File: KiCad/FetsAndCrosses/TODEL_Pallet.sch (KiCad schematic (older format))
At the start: 2 parts, among them Q1 BSS84, Q2 2N7002

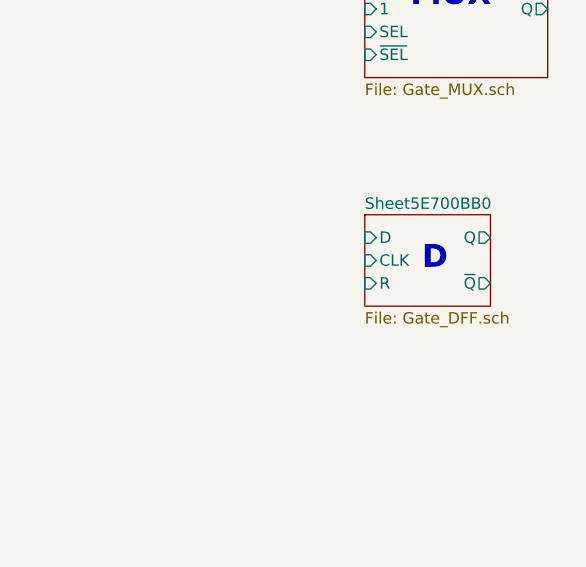
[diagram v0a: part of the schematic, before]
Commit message: Reworked everything to use Buses
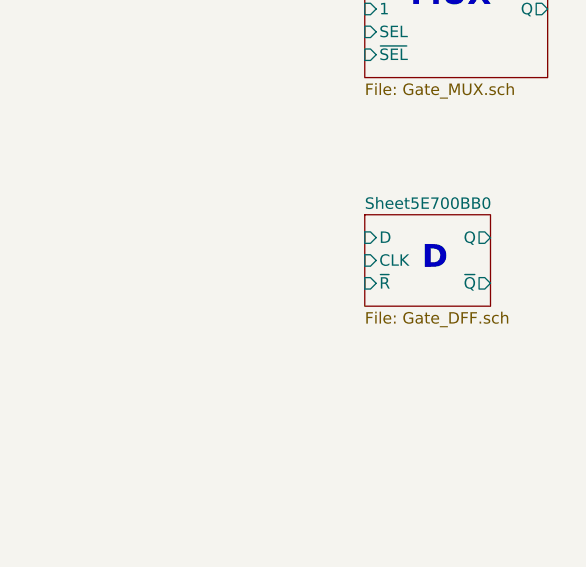
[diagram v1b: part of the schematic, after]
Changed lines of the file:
@@
 $Descr A4 11693 8268
 encoding utf-8
-Sheet 169 215
+Sheet 131 400
 Title ""
 Date ""
@@
 F2 "D" I L 8200 2100 50
 F3 "CLK" I L 8200 2200 50
-F4 "R" I L 8200 2300 50
-F5 "Q" O R 8750 2100 50
-F6 "~Q" O R 8750 2300 50
+F4 "Q" O R 8750 2100 50
+F5 "~Q" O R 8750 2300 50
+F6 "~R" I L 8200 2300 50
 $EndSheet
 Text Notes 8400 1100 0    100  ~ 20

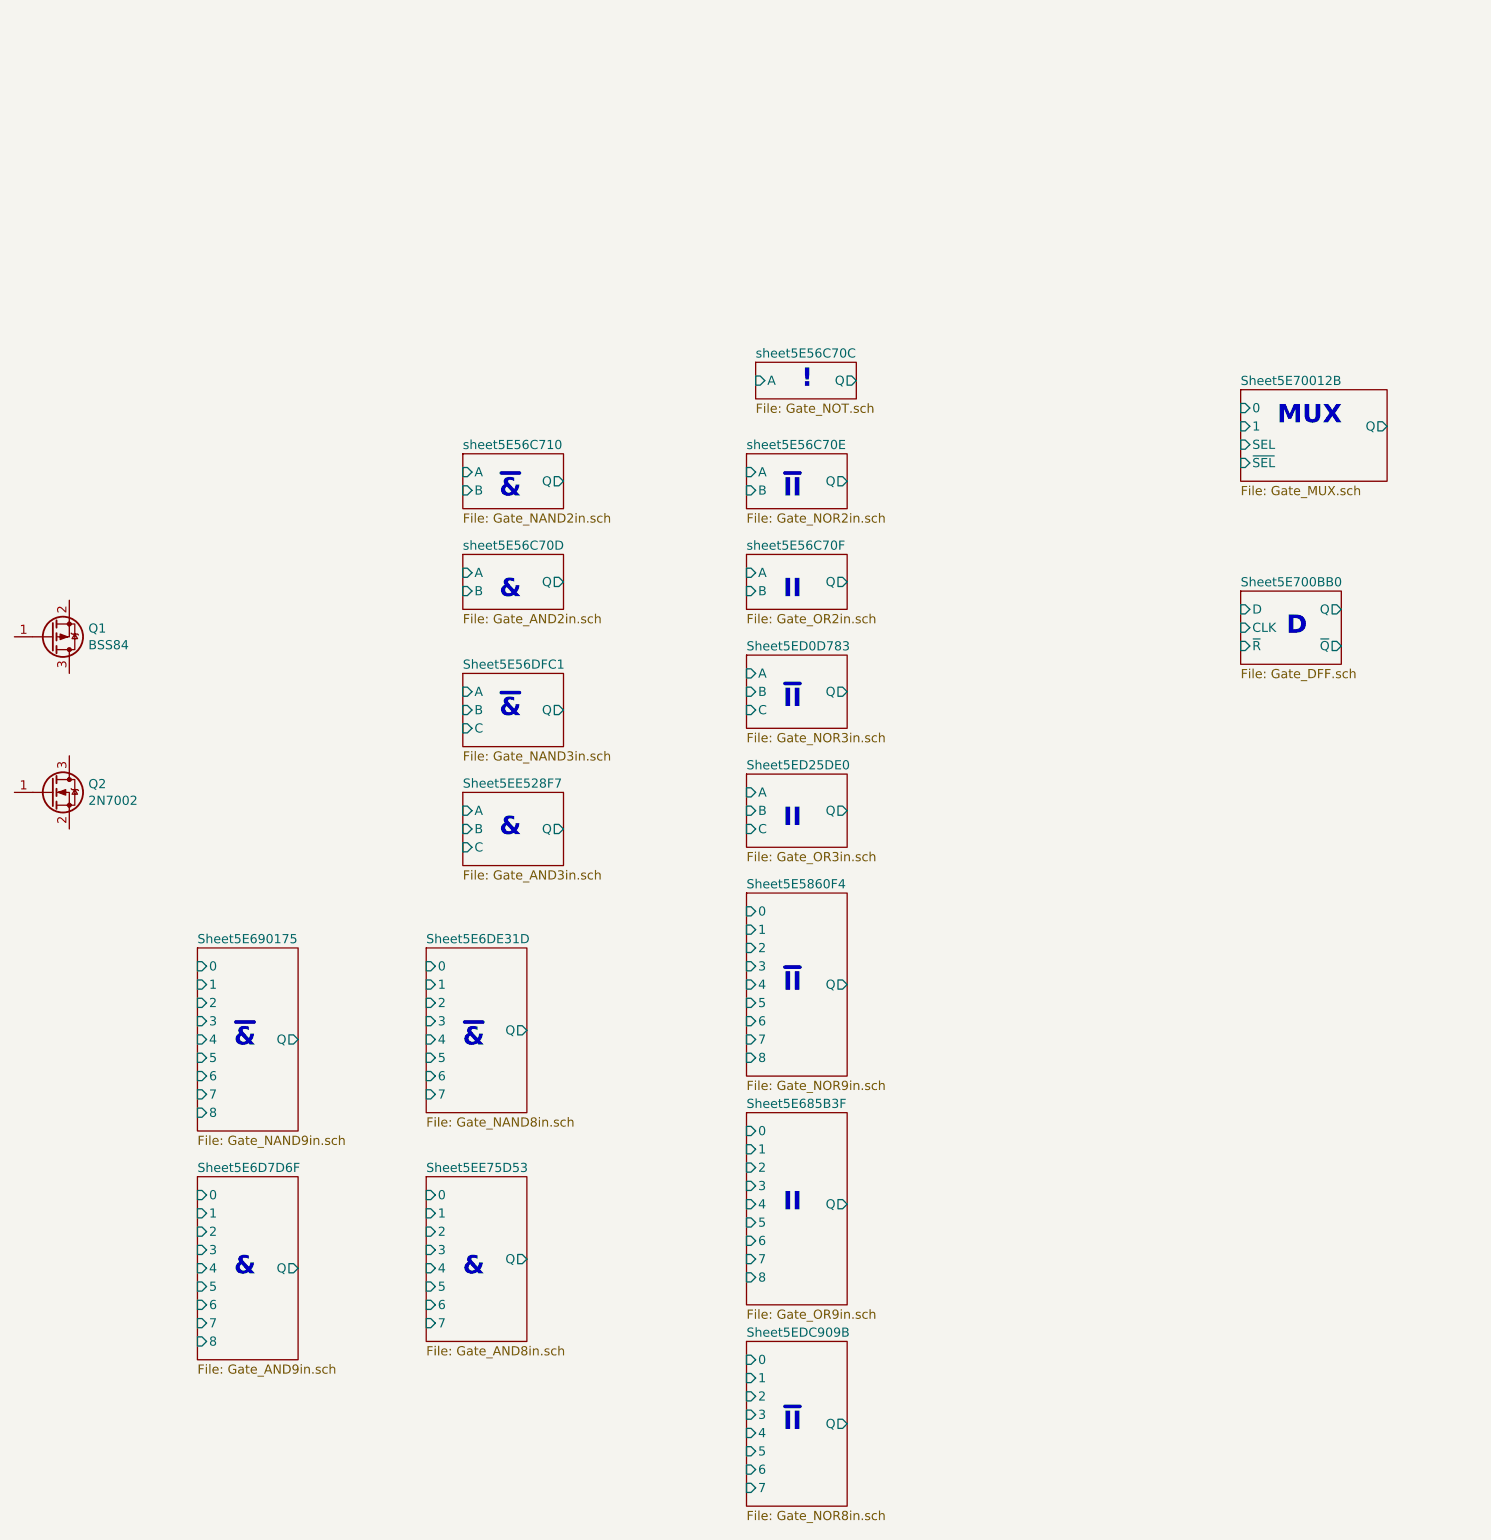
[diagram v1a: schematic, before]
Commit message: Schematic Done, Footprints assigned, ERC OK.
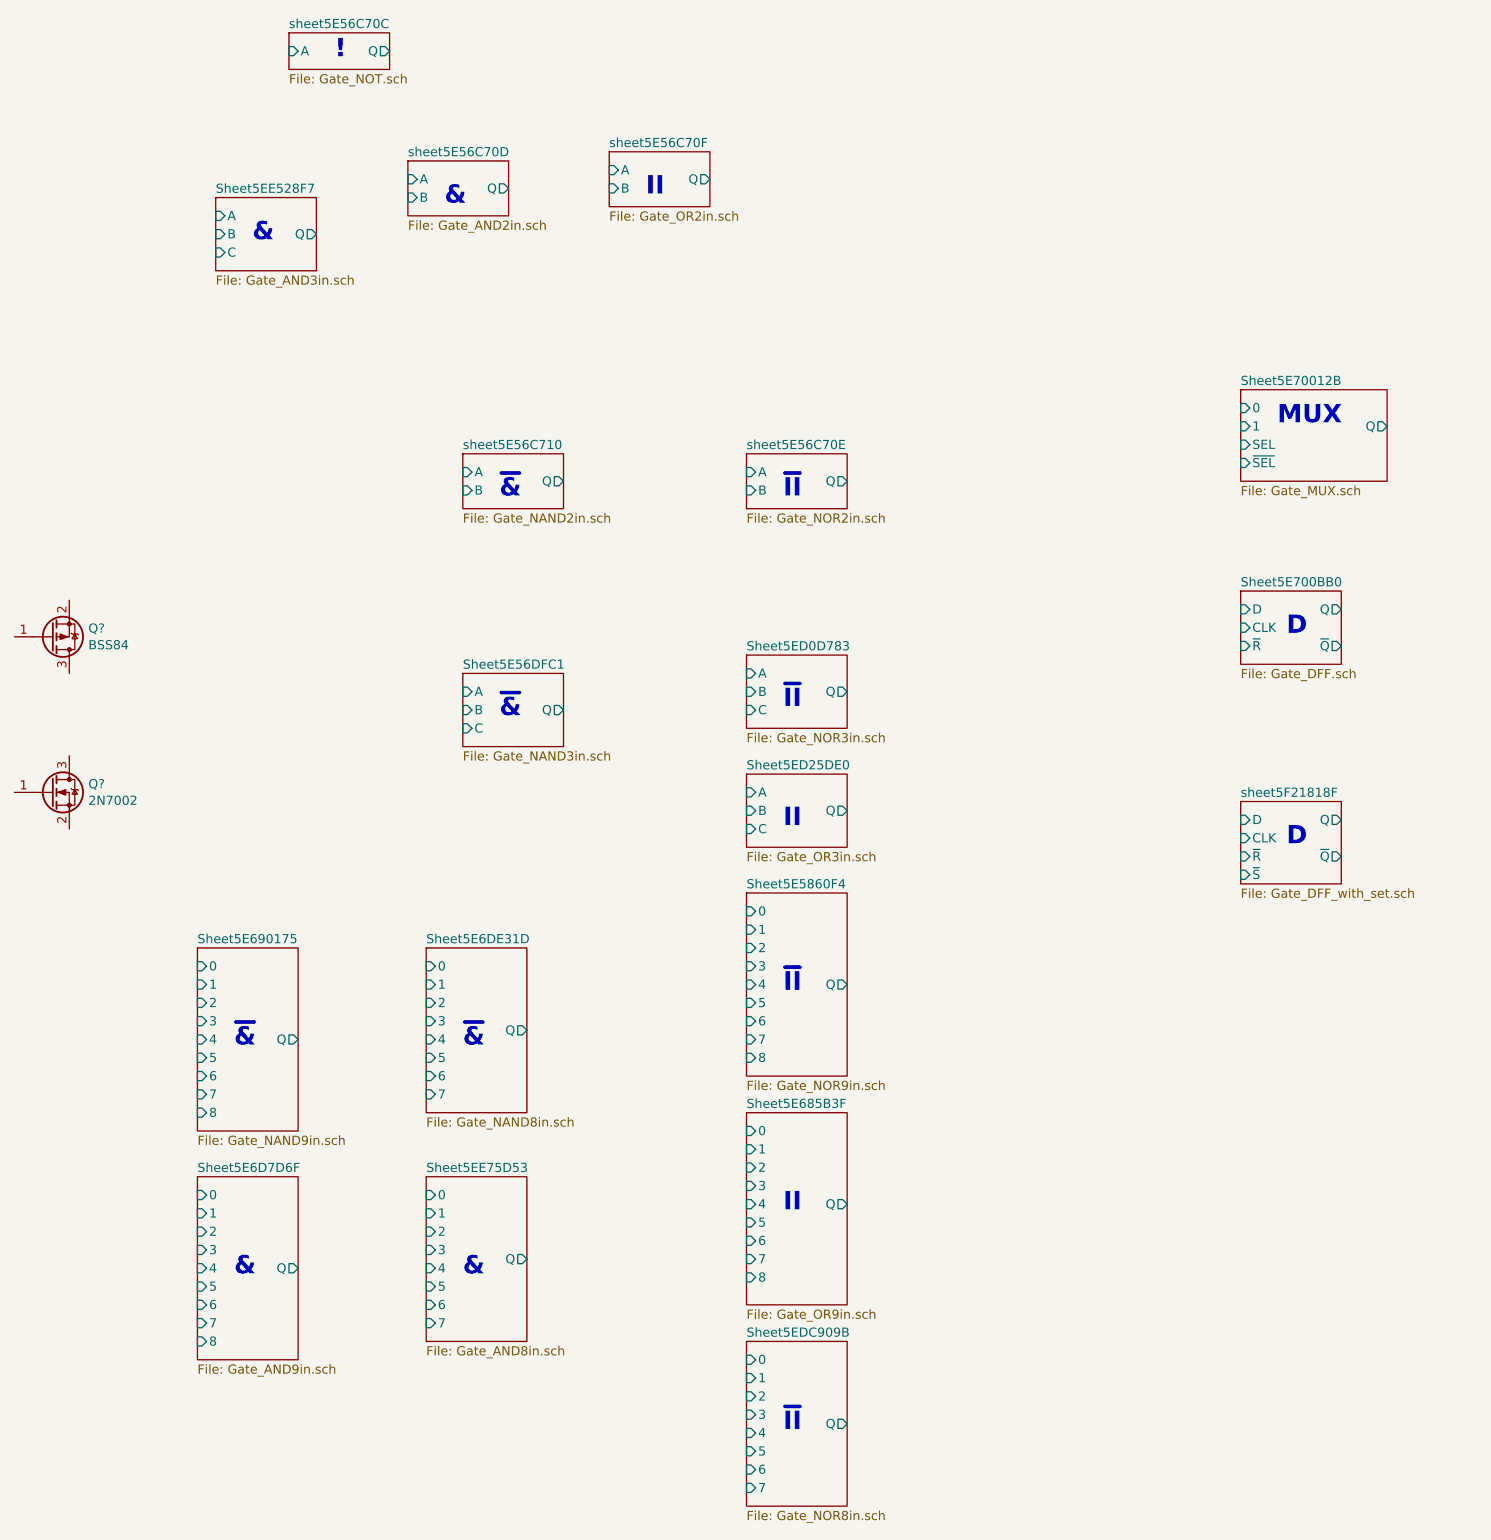
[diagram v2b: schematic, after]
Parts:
- renumbered Q1 to Q?, Q2 to Q?
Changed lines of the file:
@@
 $Descr A4 11693 8268
 encoding utf-8
-Sheet 131 400
+Sheet 159 435
 Title ""
 Date ""
@@
 $EndDescr
 $Sheet
-S 5550 750  550  200
+S 3000 -1050 550  200
 U 5E56C714
 F0 "sheet5E56C70C" 50
 F1 "Gate_NOT.sch" 50
-F2 "A" I L 5550 850 50
-F3 "Q" O R 6100 850 50
-$EndSheet
-Text Notes 5800 900  0    100  ~ 20
+F2 "A" I L 3000 -950 50
+F3 "Q" O R 3550 -950 50
+$EndSheet
+Text Notes 3250 -900 0    100  ~ 20
 !
 $Comp
@@
 AR Path="/5E53AD22/5E550B0F/5E56C71B" Ref="Q?"  Part="1"
 AR Path="/5E56C71B" Ref="Q?"  Part="1"
-AR Path="/5E56BA74/5E56C71B" Ref="Q1"  Part="1"
-F 0 "Q1" H 1904 2204 50  0000 L CNN
+AR Path="/5E56BA74/5E56C71B" Ref="Q?"  Part="1"
+F 0 "Q?" H 1904 2204 50  0000 L CNN
 F 1 "BSS84" H 1904 2295 50  0000 L CNN
 F 2 "" H 1900 2350 50  0001 C CNN
@@
 AR Path="/5E53AD22/5E550B0F/5E56C721" Ref="Q?"  Part="1"
 AR Path="/5E56C721" Ref="Q?"  Part="1"
-AR Path="/5E56BA74/5E56C721" Ref="Q2"  Part="1"
-F 0 "Q2" H 1904 3146 50  0000 L CNN
+AR Path="/5E56BA74/5E56C721" Ref="Q?"  Part="1"
+F 0 "Q?" H 1904 3146 50  0000 L CNN
 F 1 "2N7002" H 1904 3055 50  0000 L CNN
 F 2 "" H 1900 3200 50  0001 C CNN
@@
 Text Notes 4150 1500 0    100  ~ 20
 ~&
-Text Notes 4150 2050 0    100  ~ 20
+Text Notes 3850 -100 0    100  ~ 20
 &
 $Sheet
-S 3950 1800 550  300
+S 3650 -350 550  300
 U 5E56C728
 F0 "sheet5E56C70D" 50
 F1 "Gate_AND2in.sch" 50
-F2 "A" I L 3950 1900 50
-F3 "B" I L 3950 2000 50
-F4 "Q" O R 4500 1950 50
+F2 "A" I L 3650 -250 50
+F3 "B" I L 3650 -150 50
+F4 "Q" O R 4200 -200 50
 $EndSheet
 $Sheet
@@
 $EndSheet
 $Sheet
-S 5500 1800 550  300
+S 4750 -400 550  300
 U 5E56C732
 F0 "sheet5E56C70F" 50
 F1 "Gate_OR2in.sch" 50
-F2 "A" I L 5500 1900 50
-F3 "B" I L 5500 2000 50
-F4 "Q" O R 6050 1950 50
+F2 "A" I L 4750 -300 50
+F3 "B" I L 4750 -200 50
+F4 "Q" O R 5300 -250 50
 $EndSheet
 $Sheet
@@
 Text Notes 5700 1500 0    100  ~ 20
 ~II
-Text Notes 5700 2050 0    100  ~ 20
+Text Notes 4950 -150 0    100  ~ 20
 II
 $Sheet
@@
 ~II
 $Sheet
-S 3950 3100 550  400
+S 2600 -150 550  400
 U 5EE528F8
 F0 "Sheet5EE528F7" 50
 F1 "Gate_AND3in.sch" 50
-F2 "A" I L 3950 3200 50
-F3 "B" I L 3950 3300 50
-F4 "C" I L 3950 3400 50
-F5 "Q" O R 4500 3300 50
-$EndSheet
-Text Notes 4150 3350 0    100  ~ 20
+F2 "A" I L 2600 -50 50
+F3 "B" I L 2600 50  50
+F4 "C" I L 2600 150 50
+F5 "Q" O R 3150 50  50
+$EndSheet
+Text Notes 2800 100  0    100  ~ 20
 &
 $Sheet
@@
 F6 "~SEL" I L 8200 1300 50
 $EndSheet
+Text Notes 8450 3400 0    100  ~ 20
+D
+$Sheet
+S 8200 3150 550  450
+U 5F218196
+F0 "sheet5F21818F" 50
+F1 "Gate_DFF_with_set.sch" 50
+F2 "D" I L 8200 3250 50
+F3 "CLK" I L 8200 3350 50
+F4 "Q" O R 8750 3250 50
+F5 "~Q" O R 8750 3450 50
+F6 "~R" I L 8200 3450 50
+F7 "~S" I L 8200 3550 50
+$EndSheet
 $EndSCHEMATC
